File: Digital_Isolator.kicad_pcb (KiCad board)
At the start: 2 copper layers, 20 parts, among them J1 Conn_01x07, J2 Conn_01x07, J3 Conn_01x02_Male, J4 Conn_01x07, J5 Conn_01x07, J6 Conn_01x02_Male, U1 ADuM1410, U2 ADuM1410, U3 ADuM1410, U5 AP2127N3-1.5

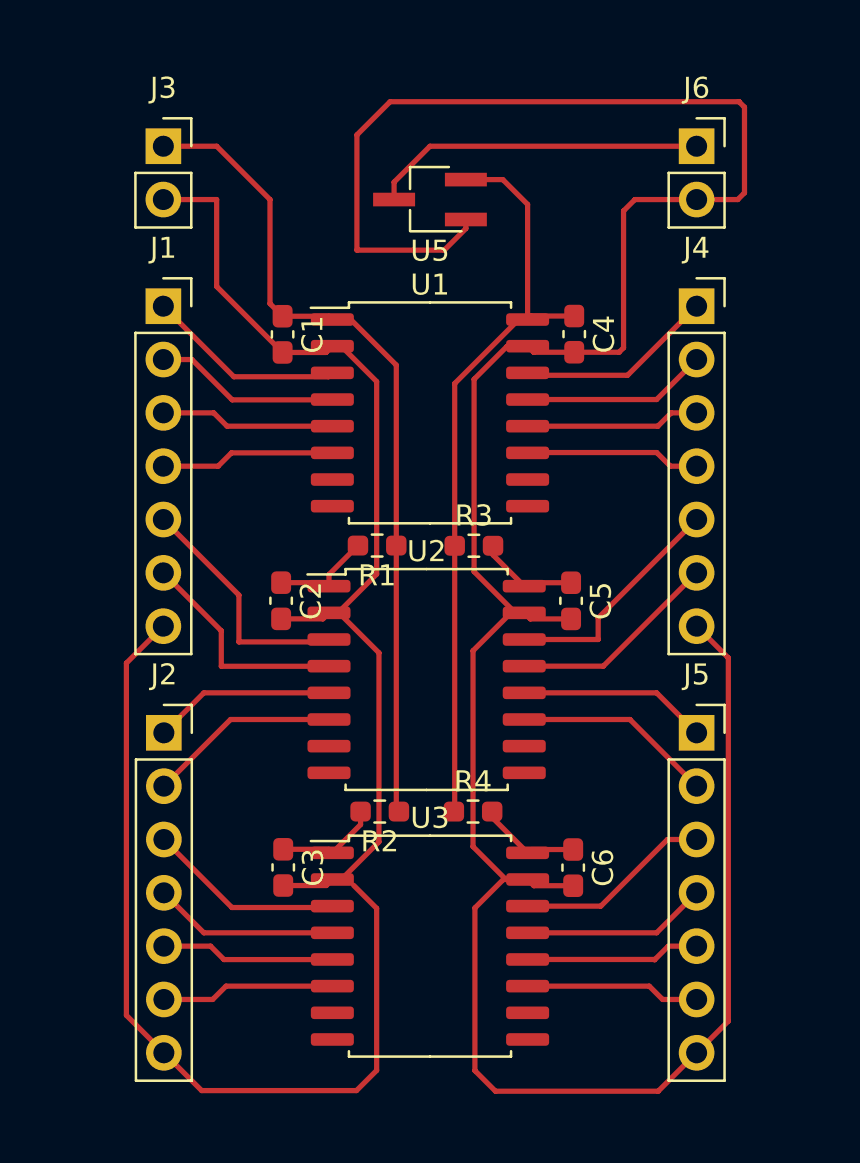
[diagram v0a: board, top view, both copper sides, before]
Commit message: Add capacitor C7
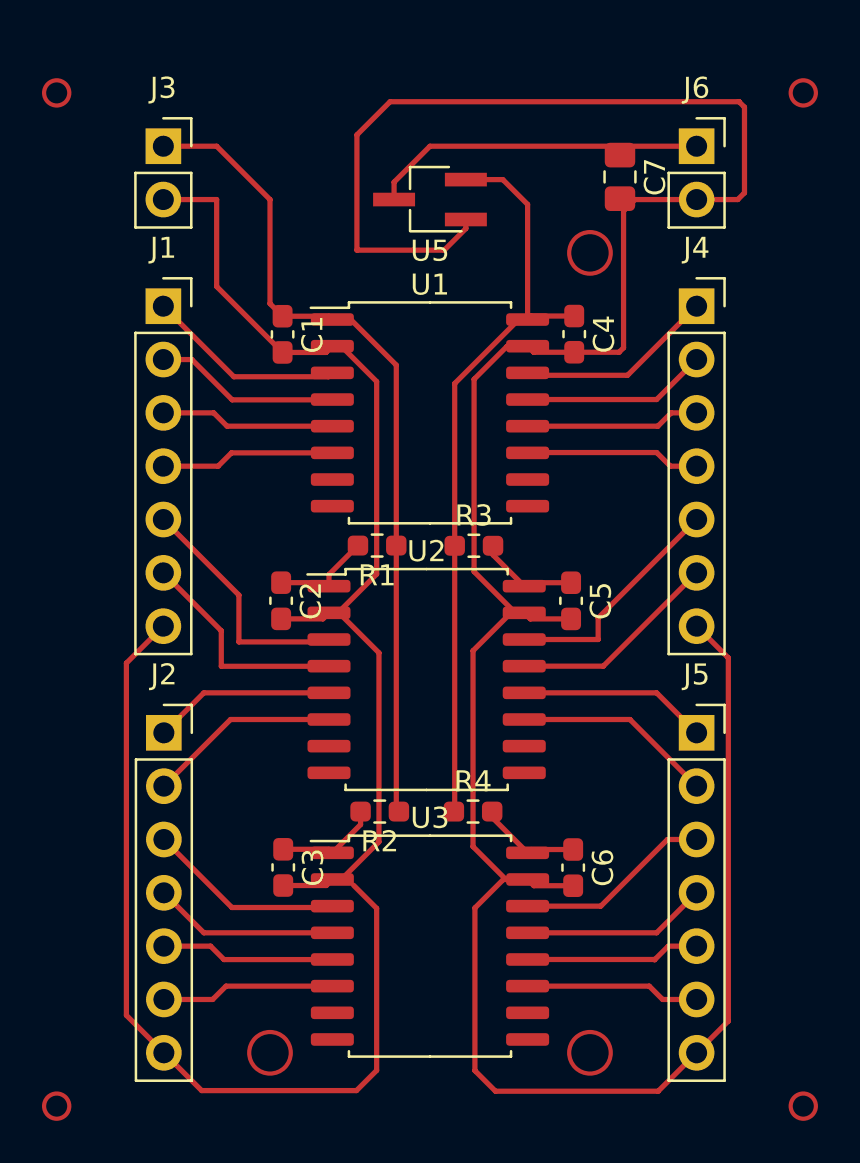
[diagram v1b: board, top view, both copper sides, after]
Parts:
- added C7: C, Capacitor_SMD:C_0805_2012Metric_Pad1.18x1.45mm_HandSolder, F.Cu at (125.9, 62.4)
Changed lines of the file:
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@@
+    )
+  )
+  (footprint "Capacitor_SMD:C_0805_2012Metric_Pad1.18x1.45mm_HandSolder" (layer "F.Cu")
+    (at 125.89 62.42 -90)
+    (descr "Capacitor SMD 0805 (2012 Metric), square (rectangular) end terminal, IPC_7351 nominal with elongated pad for handsoldering. (Body size source: IPC-SM-782 page 76, https://www.pcb-3d.com/wordpress/wp-content/uploads/ipc-sm-782a_amendment_1_and_2.pdf, https://docs.google.com/spreadsheets/d/1BsfQQcO9C6DZCsRaXUlFlo91Tg2WpOkGARC1WS5S8t0/edit?usp=sharing), generated with kicad-footprint-generator")
+    (tags "capacitor handsolder")
+    (property "Sheetfile" "Digital_Isolator.kicad_sch")
+    (property "Sheetname" "")
+    (attr smd)
+    (fp_text reference "C7" (at 0 -1.68 -90) (layer "F.SilkS")
+      (effects (font (size 1 1) (thickness 0.15)))
+    )
+    (fp_text value "C" (at 0 1.68 -90) (layer "F.Fab")
+      (effects (font (size 1 1) (thickness 0.15)))
+    )
+    (fp_text user "${REFERENCE}" (at 0 0 -90) (layer "F.Fab")
+      (effects (font (size 0.5 0.5) (thickness 0.08)))
+    )
+    (fp_line (start -0.261252 -0.735) (end 0.261252 -0.735) (layer "F.SilkS") (width 0.12))
+    (fp_line (start -0.261252 0.735) (end 0.261252 0.735) (layer "F.SilkS") (width 0.12))
+    (fp_line (start -1.88 -0.98) (end 1.88 -0.98) (layer "F.CrtYd") (width 0.05))
+    (fp_line (start 1.88 0.98) (end -1.88 0.98) (layer "F.CrtYd") (width 0.05))
+    (fp_line (start 1.88 -0.98) (end 1.88 0.98) (layer "F.CrtYd") (width 0.05))
+    (fp_line (start -1.88 0.98) (end -1.88 -0.98) (layer "F.CrtYd") (width 0.05))
+    (fp_line (start 1 0.625) (end -1 0.625) (layer "F.Fab") (width 0.1))
+    (fp_line (start -1 -0.625) (end 1 -0.625) (layer "F.Fab") (width 0.1))
+    (fp_line (start 1 -0.625) (end 1 0.625) (layer "F.Fab") (width 0.1))
+    (fp_line (start -1 0.625) (end -1 -0.625) (layer "F.Fab") (width 0.1))
+    (pad "1" smd roundrect (at -1.0375 0 270) (size 1.175 1.45) (layers "F.Cu" "F.Paste" "F.Mask") (roundrect_rratio 0.212766)
+      (net 45 "Net-(U5-Pad3)") (pintype "passive"))
+    (pad "2" smd roundrect (at 1.0375 0 270) (size 1.175 1.45) (layers "F.Cu" "F.Paste" "F.Mask") (roundrect_rratio 0.212766)
+      (net 14 "GND2") (pintype "passive"))
+    (model "${KICAD6_3DMODEL_DIR}/Capacitor_SMD.3dshapes/C_0805_2012Metric.wrl"
+      (offset (xyz 0 0 0))
+      (scale (xyz 1 1 1))
+      (rotate (xyz 0 0 0))
     )
   )
@@
     )
   )
+  (gr_circle (center 99.06 58.42) (end 99.08 59.02) (layer "F.Cu") (width 0.2) (fill none))
+  (gr_circle (center 134.62 58.42) (end 134.62 58.42) (layer "F.Cu") (width 0.2) (fill none))
+  (gr_circle (center 124.46 104.14) (end 124.48 105.13) (layer "F.Cu") (width 0.2) (fill none))
+  (gr_circle (center 109.22 104.14) (end 109.24 105.13) (layer "F.Cu") (width 0.2) (fill none))
+  (gr_circle (center 134.62 58.42) (end 134.64 59.02) (layer "F.Cu") (width 0.2) (fill none))
+  (gr_circle (center 124.46 104.14) (end 124.46 104.14) (layer "F.Cu") (width 0.2) (fill none))
+  (gr_circle (center 99.06 106.68) (end 99.08 107.28) (layer "F.Cu") (width 0.2) (fill none))
+  (gr_circle (center 124.46 66.04) (end 124.48 67.03) (layer "F.Cu") (width 0.2) (fill none))
+  (gr_circle (center 109.22 104.14) (end 109.22 104.14) (layer "F.Cu") (width 0.2) (fill none))
+  (gr_circle (center 124.46 66.04) (end 124.46 66.04) (layer "F.Cu") (width 0.2) (fill none))
+  (gr_circle (center 134.62 106.68) (end 134.64 107.28) (layer "F.Cu") (width 0.2) (fill none))
   (segment (start 106.68 60.96) (end 104.14 60.96) (width 0.25) (layer "F.Cu") (net 1))
   (segment (start 109.22 63.5) (end 106.68 60.96) (width 0.25) (layer "F.Cu") (net 1))
@@
   (segment (start 120.695 83.185) (end 118.89 84.99) (width 0.25) (layer "F.Cu") (net 14))
   (segment (start 131.82 63.18) (end 131.82 59.1) (width 0.25) (layer "F.Cu") (net 14))
+  (segment (start 126.6 63.5) (end 126.22 63.88) (width 0.25) (layer "F.Cu") (net 14))
   (segment (start 131.05 102.63) (end 131.05 85.33) (width 0.25) (layer "F.Cu") (net 14))
   (segment (start 129.54 104.14) (end 131.05 102.63) (width 0.25) (layer "F.Cu") (net 14))
@@
   (segment (start 120.335 95.885) (end 118.98 97.24) (width 0.25) (layer "F.Cu") (net 14))
   (segment (start 123.66 96.1825) (end 121.7875 96.1825) (width 0.25) (layer "F.Cu") (net 14))
-  (segment (start 126.6 63.5) (end 126.06 64.04) (width 0.25) (layer "F.Cu") (net 14))
   (segment (start 125.8475 70.7725) (end 123.71 70.7725) (width 0.25) (layer "F.Cu") (net 14))
   (segment (start 118.89 94.32) (end 120.455 95.885) (width 0.25) (layer "F.Cu") (net 14))
@@
   (segment (start 118.94 81.221751) (end 120.903249 83.185) (width 0.25) (layer "F.Cu") (net 14))
   (segment (start 118.89 84.99) (end 118.89 94.32) (width 0.25) (layer "F.Cu") (net 14))
+  (segment (start 126.22 63.88) (end 126.06 64.04) (width 0.25) (layer "F.Cu") (net 14))
   (segment (start 121.33 83.185) (end 120.695 83.185) (width 0.25) (layer "F.Cu") (net 14))
   (segment (start 126.06 70.56) (end 125.8475 70.7725) (width 0.25) (layer "F.Cu") (net 14))

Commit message: Add files via upload
Change to 0805 SMD instead 0603
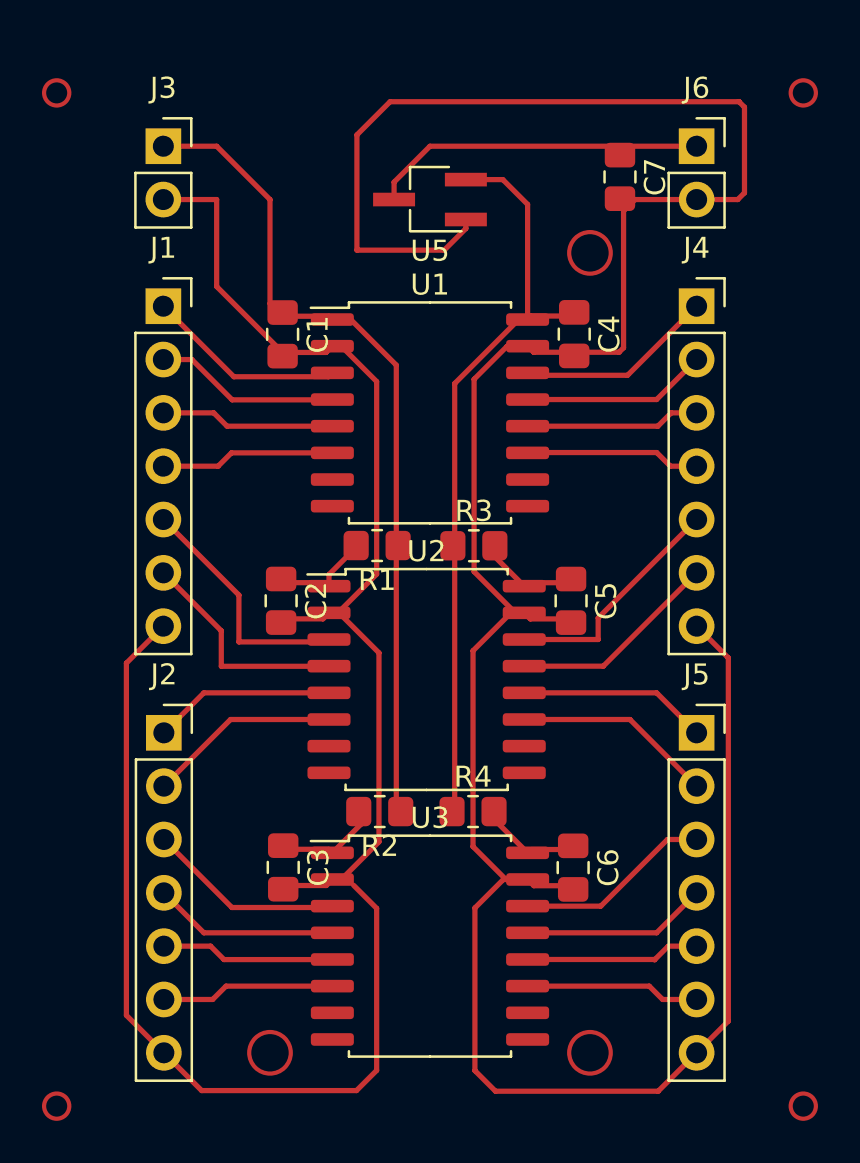
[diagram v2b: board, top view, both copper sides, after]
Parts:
- C1, C2, C3, C4, C5, C6: footprint Capacitor_SMD:C_0603_1608Metric_Pad1.08x0.95mm_HandSolder -> Capacitor_SMD:C_0805_2012Metric_Pad1.18x1.45mm_HandSolder
- R1, R2, R3, R4: footprint Resistor_SMD:R_0603_1608Metric_Pad0.98x0.95mm_HandSolder -> Resistor_SMD:R_0805_2012Metric_Pad1.20x1.40mm_HandSolder

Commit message: Add files via upload
Bug fixes
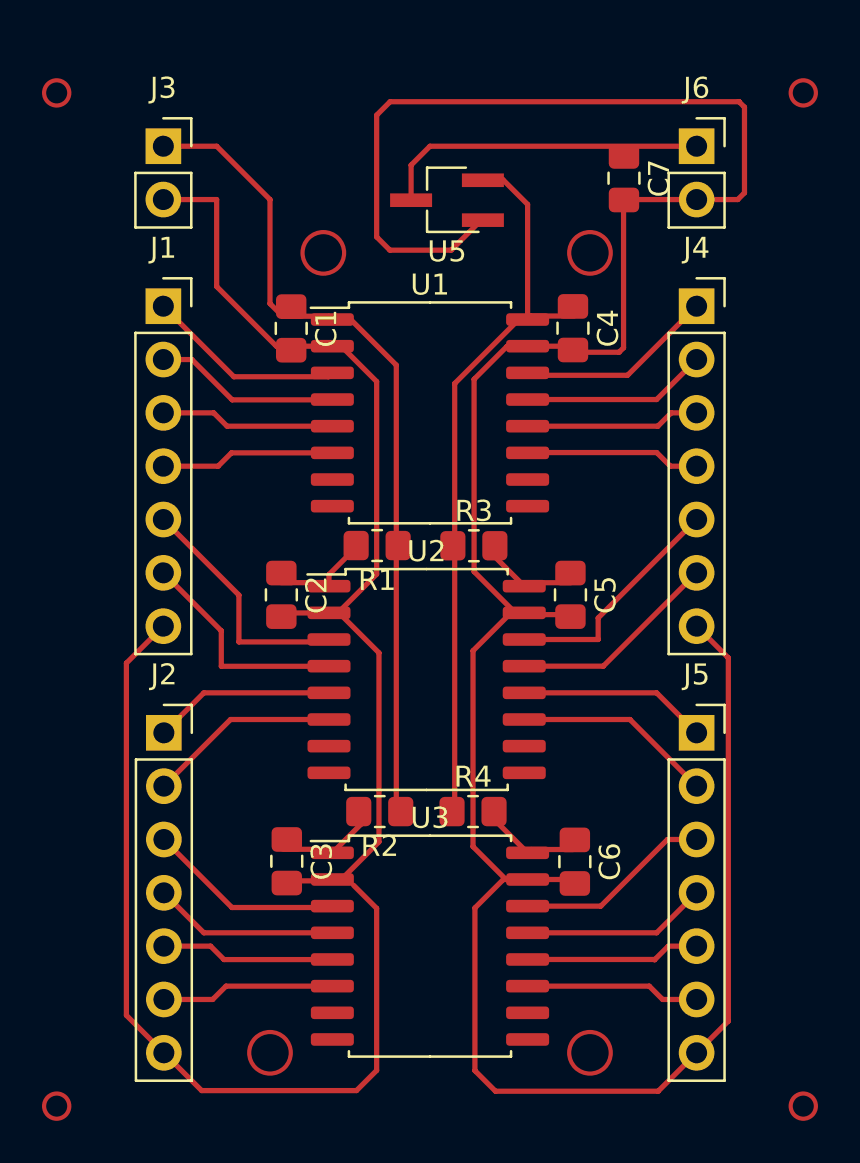
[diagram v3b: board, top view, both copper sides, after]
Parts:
- moved U5 0.81 mm to (117.7, 63.5)
- moved C1 0.50 mm to (110.2, 69.6)
- moved C3 0.34 mm to (110.0, 95.0)
- moved C6 0.29 mm to (123.7, 95.0)
- moved C4 0.29 mm to (123.7, 69.6)
- moved C5 0.29 mm to (123.5, 82.3)
- moved C2 0.28 mm to (109.8, 82.3)
- moved C7 0.20 mm to (126.1, 62.5)
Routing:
- net GND2: track 132.9 -> 131.7 mm

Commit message: Change distance between pins for 0.6 mm tool
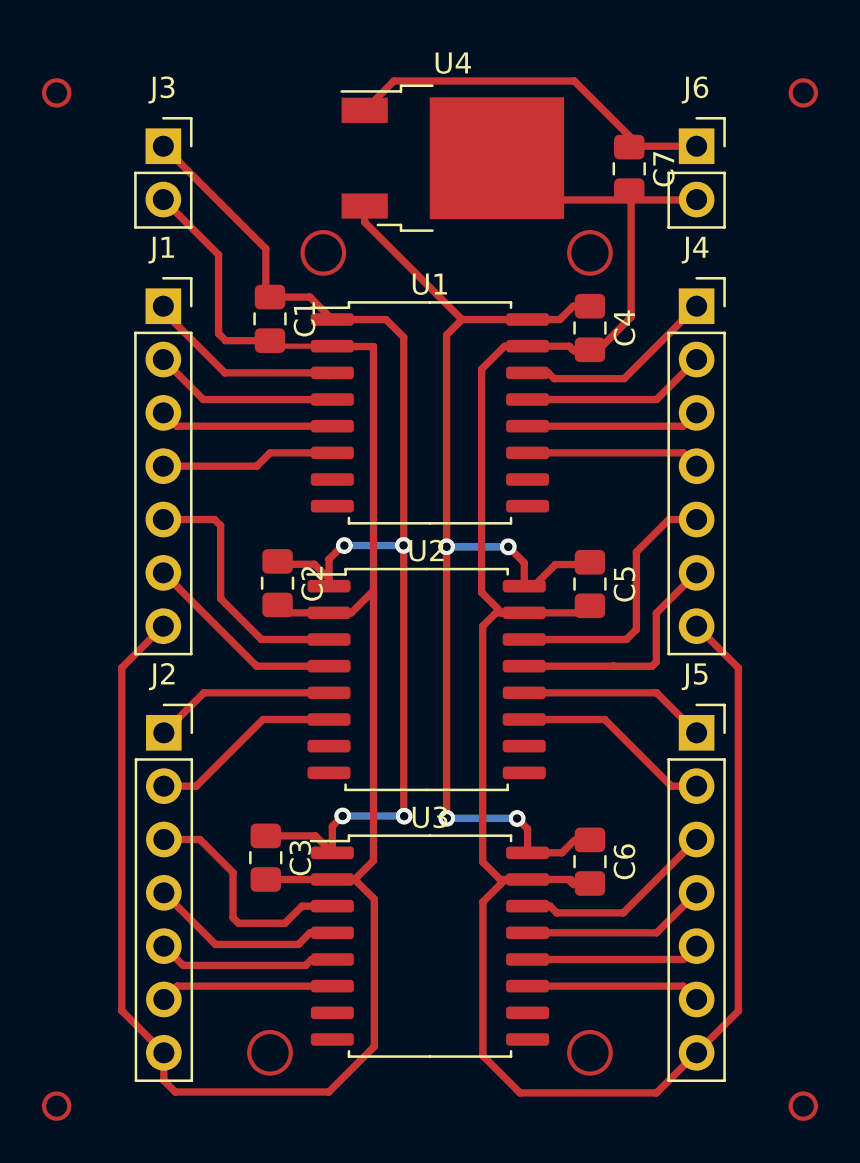
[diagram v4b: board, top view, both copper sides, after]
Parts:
- removed R1, R2, R3, R4: R, Resistor_SMD:R_0805_2012Metric_Pad1.20x1.40mm_HandSolder
- removed U5: AP2127N3-1.5, Package_TO_SOT_SMD:TSOT-23_HandSoldering
- added U4: MC78M05_TO252, Package_TO_SOT_SMD:TO-252-2, F.Cu at (117.9, 61.5)
- moved C1 1.11 mm to (109.2, 69.2)
- moved C5 1.06 mm to (124.5, 81.8)
- moved C3 1.01 mm to (109.0, 94.8)
- moved C4 0.81 mm to (124.5, 69.6)
- moved C6 0.72 mm to (124.5, 95.0)
- moved C2 0.58 mm to (109.6, 81.8)
- moved C7 0.51 mm to (126.3, 62.0)
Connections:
- C2 pad 1: Net-(C2-Pad1) -> +3.3V
- C3 pad 1: Net-(C3-Pad1) -> +3.3V
- C4 pad 1: Net-(C4-Pad1) -> Net-(C6-Pad1)
- C5 pad 1: Net-(C5-Pad1) -> Net-(C6-Pad1)
- U1 pad 16: Net-(C4-Pad1) -> Net-(C6-Pad1)
- U2 pad 1: Net-(C2-Pad1) -> +3.3V
- U2 pad 16: Net-(C5-Pad1) -> Net-(C6-Pad1)
- U3 pad 1: Net-(C3-Pad1) -> +3.3V
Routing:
- net Net-(C6-Pad1): track 4.90 -> 55.2 mm, vias 0 -> 4
- net Net-(C4-Pad1): track 36.3 -> 0.00 mm
- net GND2: track 131.7 -> 105.8 mm
- net +3.3V: track 39.9 -> 58.5 mm, vias 0 -> 4
- net Net-(C3-Pad1): track 4.93 -> 0.00 mm
- net Net-(C5-Pad1): track 4.84 -> 0.00 mm
- net Net-(C2-Pad1): track 4.62 -> 0.00 mm
- net GND1: track 91.5 -> 96.1 mm
- net Net-(J2-Pad3): track 9.39 -> 11.4 mm
- net Net-(J4-Pad5): track 11.2 -> 12.7 mm
- net Net-(J4-Pad6): track 10.1 -> 11.4 mm
- net Net-(C7-Pad1): track 16.4 -> 17.5 mm
- net Net-(J1-Pad6): track 10.7 -> 9.74 mm
- net Net-(J1-Pad5): track 11.7 -> 12.5 mm
